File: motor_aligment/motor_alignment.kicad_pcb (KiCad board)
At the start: 2 copper layers, 110 x 80 mm, 25 parts, among them J1 PWR_24V_IN, J2 SENSOR_IN, J3 LCD_I2C, SW1 BTN, U1 LM2596S-5, U2 ADS1115, U3 ESP32-WROOM-32

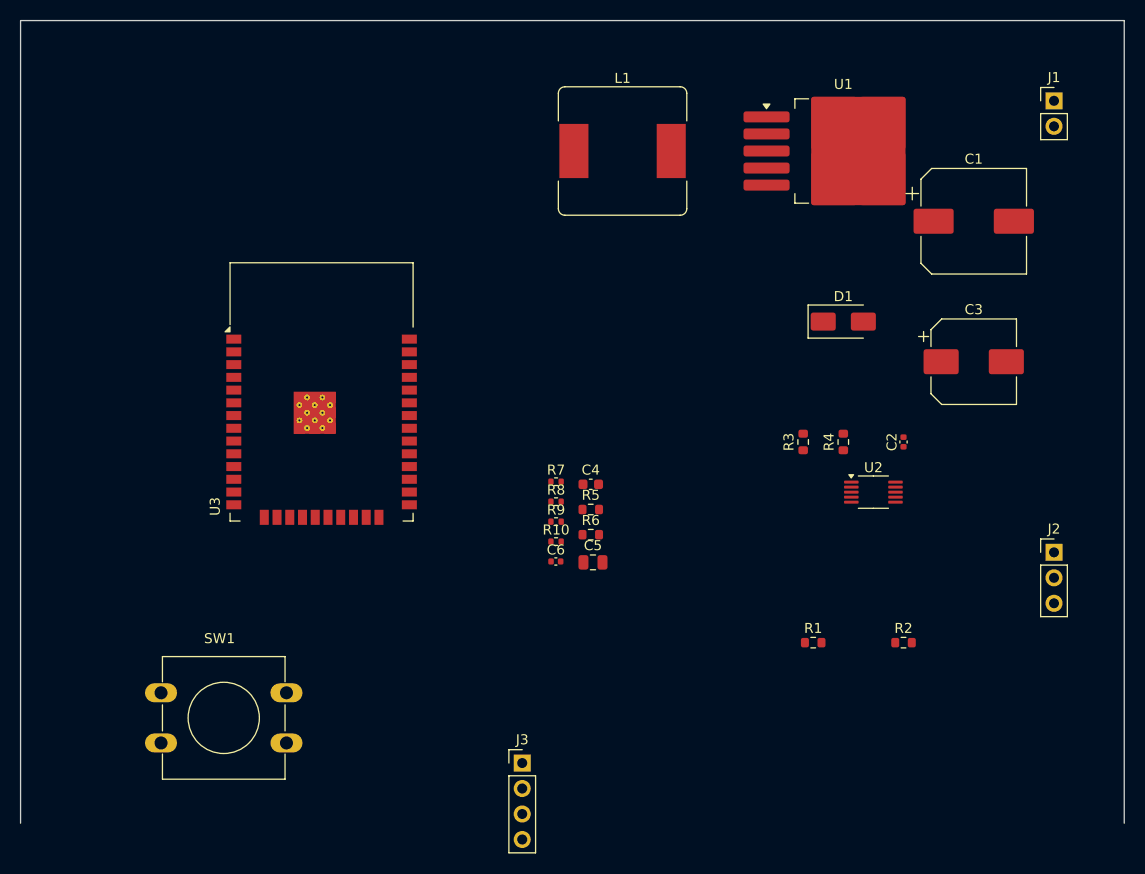
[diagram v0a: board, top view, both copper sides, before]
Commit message: Clean PCB layout: remove all traces/vias, fix component placement
- Remove all routing segments and vias (to be re-routed manually)
- Fix LCSC/MPN/Manufacturer/JLCPCB_Type properties on all 22 components
- Fix R7-R10 and C2/C6 footprints from 0402 to 0603
- Assign PinHeader_1x04 footprint to J4/J5
- Place components per LM2596 datasheet layout (pp. 31-32)
- Resolve courtyard overlaps and ESP32 antenna keepout violations
- DRC: 0 errors, 1 warning (lib_footprint_mismatch)

Co-Authored-By: Claude Sonnet 4.6 <noreply@anthropic.com>
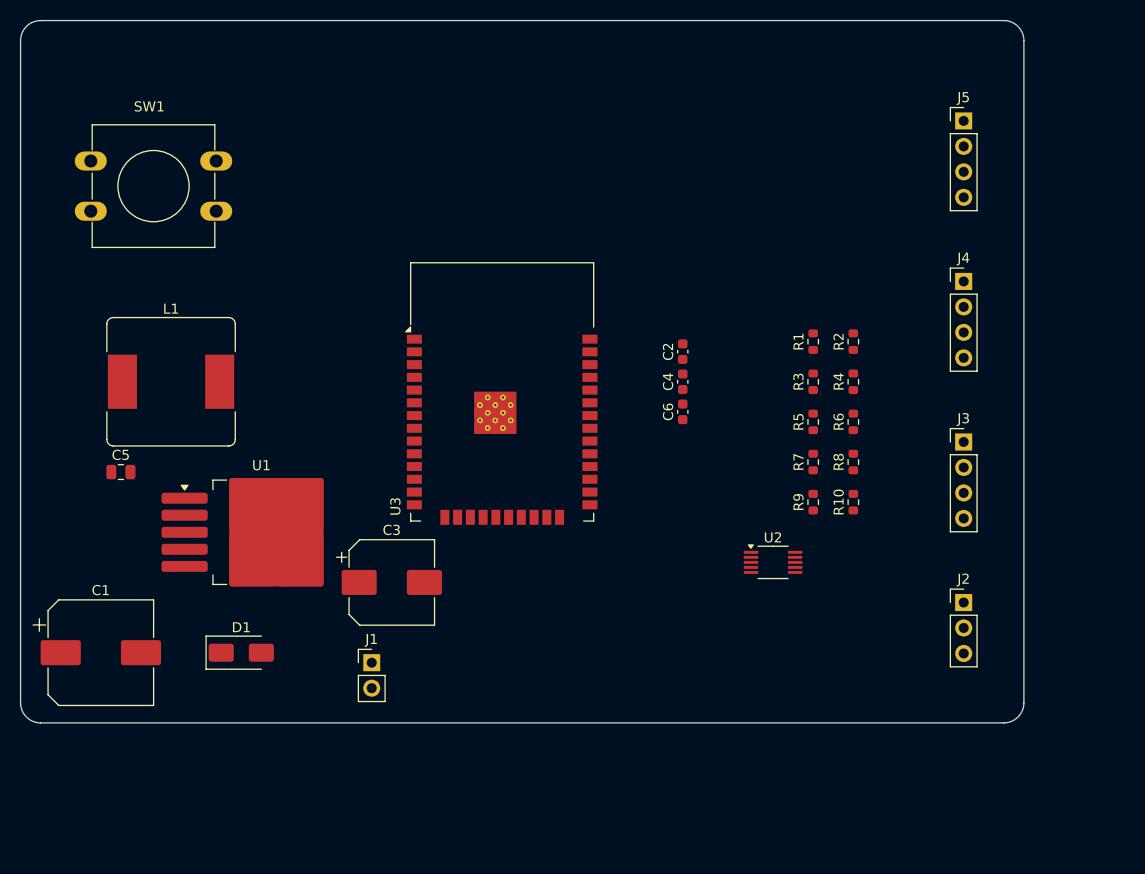
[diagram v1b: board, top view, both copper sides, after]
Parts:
- added J4: UART_DOWNLOAD, Connector_PinHeader_2.54mm:PinHeader_1x04_P2.54mm_Vertical, F.Cu at (94.0, 26.0)
- added J5: JTAG, Connector_PinHeader_2.54mm:PinHeader_1x04_P2.54mm_Vertical, F.Cu at (94.0, 10.0)
- C2, C6: footprint Capacitor_SMD:C_0402_1005Metric -> Capacitor_SMD:C_0603_1608Metric
- R10, R7, R8, R9: footprint Resistor_SMD:R_0402_1005Metric -> Resistor_SMD:R_0603_1608Metric
- moved C1 97.0 mm to (8.00, 63.0)
- moved J1 88.1 mm to (35.0, 64.0)
- moved U1 69.3 mm to (24.0, 51.0)
- moved D1 68.5 mm to (22.0, 63.0)
- moved C3 62.0 mm to (37.0, 56.0)
- moved J3 54.4 mm to (94.0, 42.0)
- moved SW1 53.5 mm to (7.00, 14.0)
- moved L1 50.5 mm to (15.0, 36.0)
- moved C5 47.9 mm to (10.0, 45.0)
- moved R2 30.4 mm to (83.0, 32.0), turned to 90 degrees
- moved R1 30.0 mm to (79.0, 32.0), turned to 90 degrees
- moved R8 29.9 mm to (83.0, 44.0), turned to 90 degrees
- moved R10 29.9 mm to (83.0, 48.0), turned to 90 degrees
- moved R6 28.5 mm to (83.0, 40.0), turned to 90 degrees
- moved R7 25.7 mm to (79.0, 44.0), turned to 90 degrees
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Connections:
- net /IO0_BOOT renamed Net-(U3-IO0)
- net /SCL renamed SCL
- net /SDA renamed SDA
- C1 pad 1: /+24V -> +24V
- C1 pad 2: /GND -> GND
- C2 pad 1: /+5V -> +5V
- C2 pad 2: /GND -> GND
- C3 pad 1: /+5V -> PWR_FLAG
- C3 pad 2: /GND -> GND
- C4 pad 2: /GND -> GND
- C5 pad 1: /+3.3V -> +3.3V
- C5 pad 2: /GND -> GND
- C6 pad 1: /+3.3V -> +3.3V
- C6 pad 2: /GND -> GND
- D1 pad 2: /GND -> GND
- J1 pad 1: /+24V -> PWR_FLAG
- J1 pad 2: /GND -> PWR_FLAG
- J2 pad 1: /+24V -> +24V
- J2 pad 3: /GND -> GND
- J3 pad 1: /+5V -> +5V
- J3 pad 2: /GND -> GND
- L1 pad 2: /+5V -> PWR_FLAG
- R10 pad 1: /JTAG_TDO -> Net-(U3-IO15)
- R10 pad 2: /IO15_JTAG -> /JTAG_TDO
- R2 pad 2: /GND -> GND
- R3 pad 1: /+3.3V -> +3.3V
- R4 pad 1: /+3.3V -> +3.3V
- R5 pad 1: /+3.3V -> PWR_FLAG
- R6 pad 1: /+3.3V -> +3.3V
- R7 pad 1: /JTAG_TDI -> Net-(U3-IO12)
- R7 pad 2: /IO12_JTAG -> /JTAG_TDI
- R8 pad 1: /JTAG_TMS -> Net-(U3-IO14)
- R8 pad 2: /IO14_JTAG -> /JTAG_TMS
- R9 pad 1: /JTAG_TCK -> Net-(U3-IO13)
- R9 pad 2: /IO13_JTAG -> /JTAG_TCK
- SW1 pad 2: /GND -> GND
- U1 pad 1: /+24V -> +24V
- U1 pad 3: /GND -> GND
- U1 pad 4: /+5V -> PWR_FLAG
- U1 pad 5: /GND -> GND
- U2 pad 1: /GND -> GND
- U2 pad 3: /GND -> GND
- U2 pad 8: /+5V -> +5V
- U3 pad 1: /GND -> GND
- U3 pad 13: /IO14_JTAG -> Net-(U3-IO14)
- U3 pad 14: /IO12_JTAG -> Net-(U3-IO12)
- U3 pad 15: /GND -> GND
- U3 pad 16: /IO13_JTAG -> Net-(U3-IO13)
- U3 pad 2: /+3.3V -> +3.3V
- U3 pad 23: /IO15_JTAG -> Net-(U3-IO15)
- U3 pad 37: unconnected-(U3-IO23-Pad37) -> /BTN
- U3 pad 38: /GND -> GND
- U3 pad 39: /GND -> GND
- U3 pad 8: /BTN -> unconnected-(U3-IO32-Pad8)
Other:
- board size 110 x 80 mm -> 100 x 70 mm

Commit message: Fix J4/J5 net assignments on PCB after schematic sync
J4 (UART_DOWNLOAD): pad1=+3.3V, pad2=UART_TX, pad3=UART_RX, pad4=GND
J5 (JTAG): pad1=JTAG_TDI, pad2=JTAG_TCK, pad3=JTAG_TMS, pad4=JTAG_TDO

Co-Authored-By: Claude Sonnet 4.6 <noreply@anthropic.com>
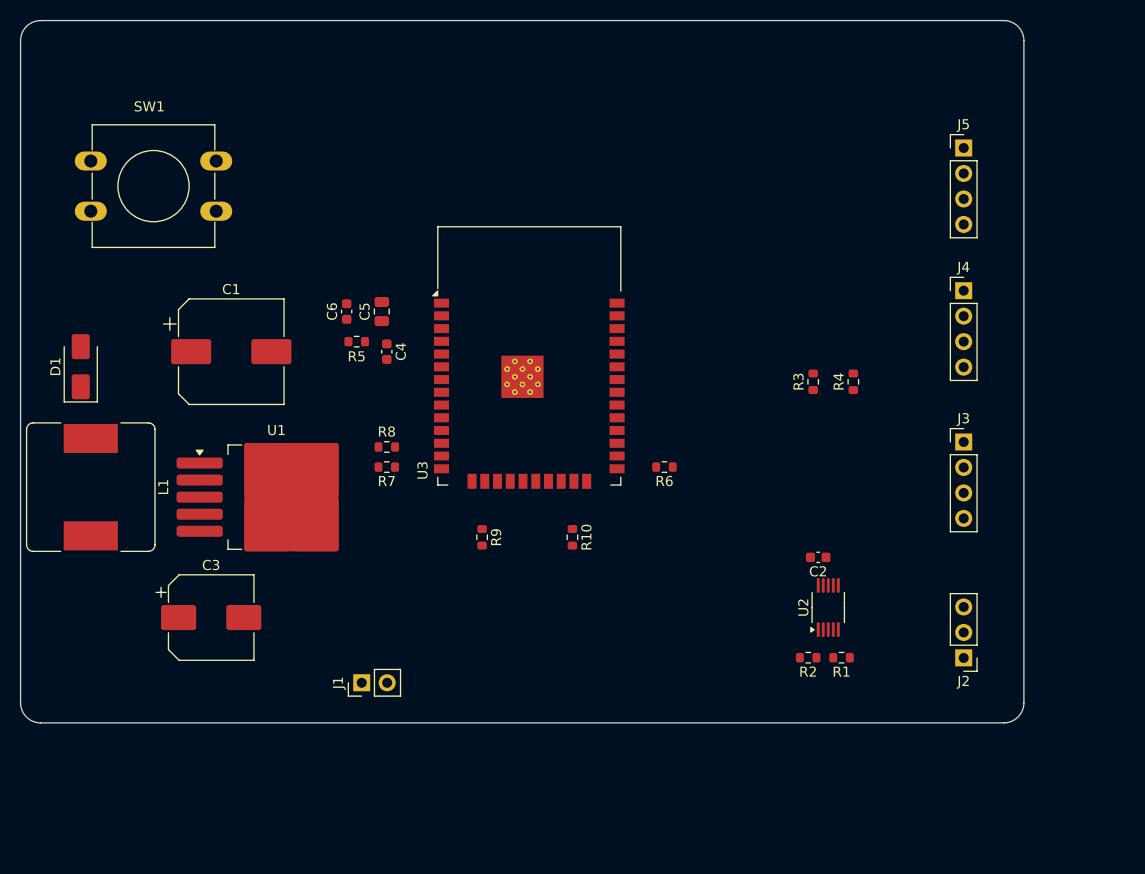
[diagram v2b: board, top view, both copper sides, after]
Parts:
- moved R8 46.5 mm to (36.5, 42.5), turned to 180 degrees
- moved R5 46.2 mm to (33.5, 32.0), turned to 0 degrees
- moved R7 42.5 mm to (36.5, 44.5), turned to 180 degrees
- moved C6 35.0 mm to (32.5, 29.0)
- moved R9 33.2 mm to (46.0, 51.5), turned to -90 degrees
- moved C1 32.7 mm to (21.0, 33.0)
- moved D1 32.7 mm to (6.00, 34.5), turned to 90 degrees
- moved R2 31.8 mm to (78.5, 63.5), turned to 180 degrees
- moved R1 31.6 mm to (81.8, 63.5), turned to 180 degrees
- moved C5 30.5 mm to (36.0, 29.0), turned to 90 degrees
- moved C4 29.7 mm to (36.5, 33.0), turned to -90 degrees
- moved R10 28.2 mm to (55.0, 51.5), turned to -90 degrees
- moved C2 24.5 mm to (79.5, 53.5), turned to 180 degrees
- moved R6 19.4 mm to (64.2, 44.5), turned to 180 degrees
- moved C3 18.3 mm to (19.0, 59.5)
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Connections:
- net SCL renamed /SCL
- net SDA renamed /SDA
- C1 pad 1: +24V -> /+24V
- C2 pad 1: +5V -> /+5V
- C3 pad 1: PWR_FLAG -> /+5V
- C5 pad 1: +3.3V -> /+3.3V
- C6 pad 1: +3.3V -> /+3.3V
- J1 pad 1: PWR_FLAG -> /+24V
- J1 pad 2: PWR_FLAG -> GND
- J2 pad 1: +24V -> /+24V
- J3 pad 1: +5V -> /+5V
- J4 pad 2: (no net) -> /UART_TX
- J4 pad 3: (no net) -> /UART_RX
- J5 pad 1: (no net) -> /JTAG_TDI
- J5 pad 2: (no net) -> /JTAG_TCK
- J5 pad 3: (no net) -> /JTAG_TMS
- J5 pad 4: (no net) -> /JTAG_TDO
- L1 pad 2: PWR_FLAG -> /+5V
- R3 pad 1: +3.3V -> /+3.3V
- R4 pad 1: +3.3V -> /+3.3V
- R5 pad 1: PWR_FLAG -> /+3.3V
- R6 pad 1: +3.3V -> /+3.3V
- U1 pad 1: +24V -> /+24V
- U1 pad 4: PWR_FLAG -> /+5V
- U2 pad 8: +5V -> /+5V
- U3 pad 2: +3.3V -> /+3.3V

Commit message: Update PCB, DSN/SES routing files and BOM export
Co-Authored-By: Claude Sonnet 4.6 <noreply@anthropic.com>
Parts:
- moved U3 11.1 mm to (61.8, 35.9)
- moved C4 11.0 mm to (47.5, 32.5)
- moved C5 11.0 mm to (47.0, 28.4)
- moved C6 11.0 mm to (43.5, 28.4)
- moved R10 11.0 mm to (66.0, 51.0)
- moved R5 11.0 mm to (44.5, 31.4)
- moved R6 11.0 mm to (75.2, 44.0)
- moved R7 11.0 mm to (47.5, 44.0)
- moved R8 11.0 mm to (47.5, 42.0)
- moved R9 11.0 mm to (57.0, 51.0)
- moved R4 9.64 mm to (75.5, 29.9), turned to 180 degrees
- moved R3 4.06 mm to (75.5, 34.0), turned to 180 degrees
- moved C1 3.54 mm to (24.5, 32.5)
- moved C3 3.54 mm to (22.5, 59.0)
- moved D1 3.54 mm to (9.50, 34.0)
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
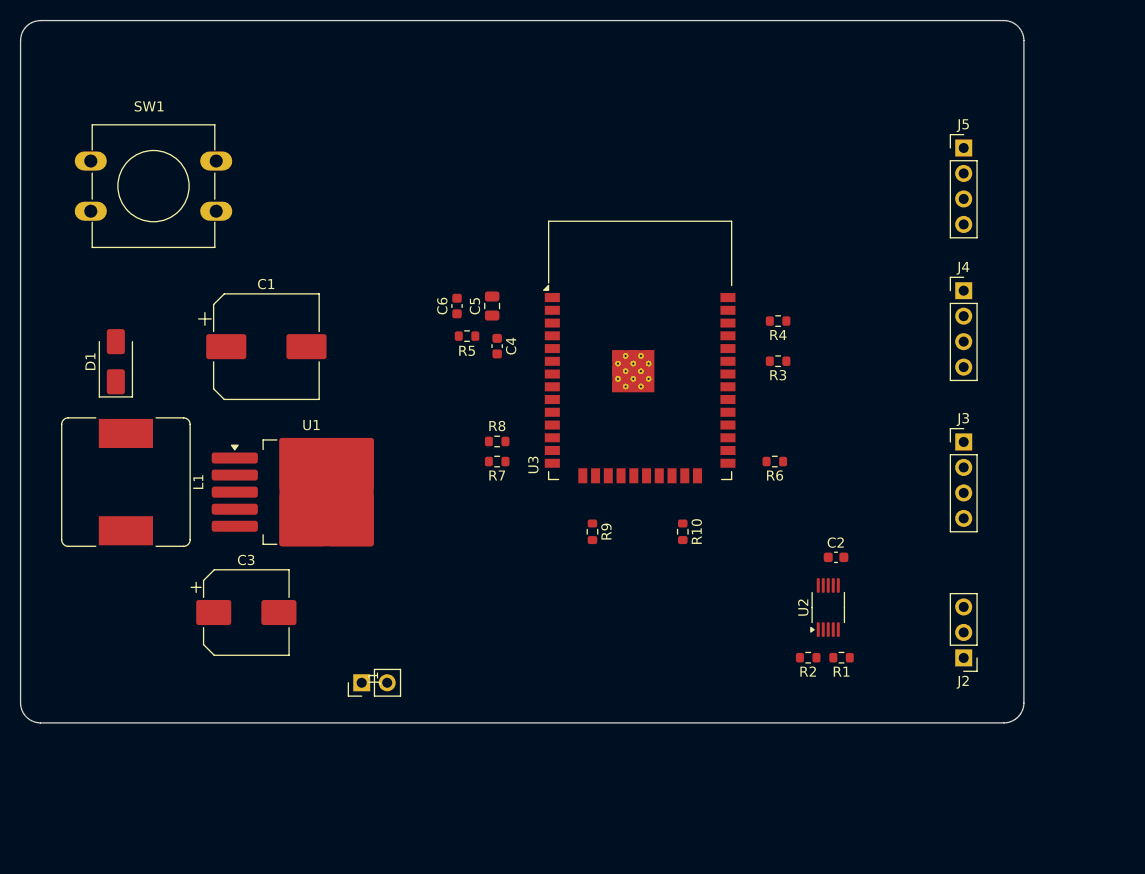
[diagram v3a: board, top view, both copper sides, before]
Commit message: Route all signal/power nets via Freerouting (GND excluded for copper pour)
- 160 tracks, 3 vias, 71 wire segments
- GND left unrouted (to be filled as copper pour)
- DRC: 0 errors, 3 warnings (silk cosmetic + lib_footprint_mismatch)

Co-Authored-By: Claude Sonnet 4.6 <noreply@anthropic.com>
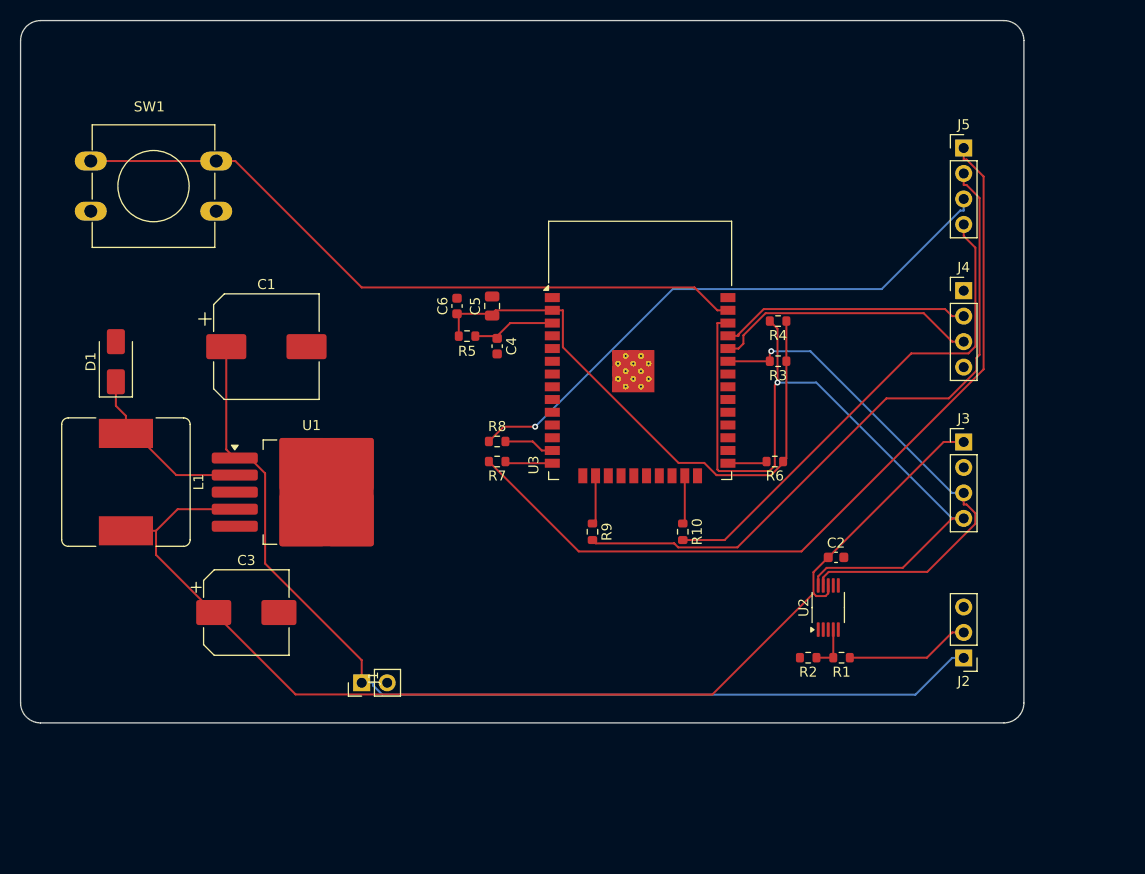
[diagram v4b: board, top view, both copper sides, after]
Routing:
- net /+5V: track 0.00 -> 114.6 mm
- net /+24V: track 0.00 -> 102.1 mm
- net /JTAG_TDI: track 0.00 -> 83.6 mm
- net /SCL: track 0.00 -> 78.5 mm, vias 0 -> 1
- net /BTN: track 0.00 -> 69.7 mm
- net /JTAG_TCK: track 0.00 -> 66.5 mm
- net /+3.3V: track 0.00 -> 58.8 mm
- net /JTAG_TMS: track 0.00 -> 58.0 mm, vias 0 -> 1
- net /SDA: track 0.00 -> 52.2 mm, vias 0 -> 1
- net /JTAG_TDO: track 0.00 -> 49.8 mm
- net /UART_RX: track 0.00 -> 26.6 mm
- net /UART_TX: track 0.00 -> 25.0 mm
- net Net-(D1-K): track 0.00 -> 18.5 mm
- net /SENSOR_OUT: track 0.00 -> 12.4 mm
- net /ESP32_EN: track 0.00 -> 8.44 mm
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
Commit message: Add GND copper pour on F.Cu and B.Cu
- Solid fill on SMD pads (thru_hole_only thermal relief)
- Thermal gap 0.1mm, bridge width 0.15mm
- DRC: 0 errors, 3 warnings (silk cosmetic + lib_footprint_mismatch)

Co-Authored-By: Claude Sonnet 4.6 <noreply@anthropic.com>
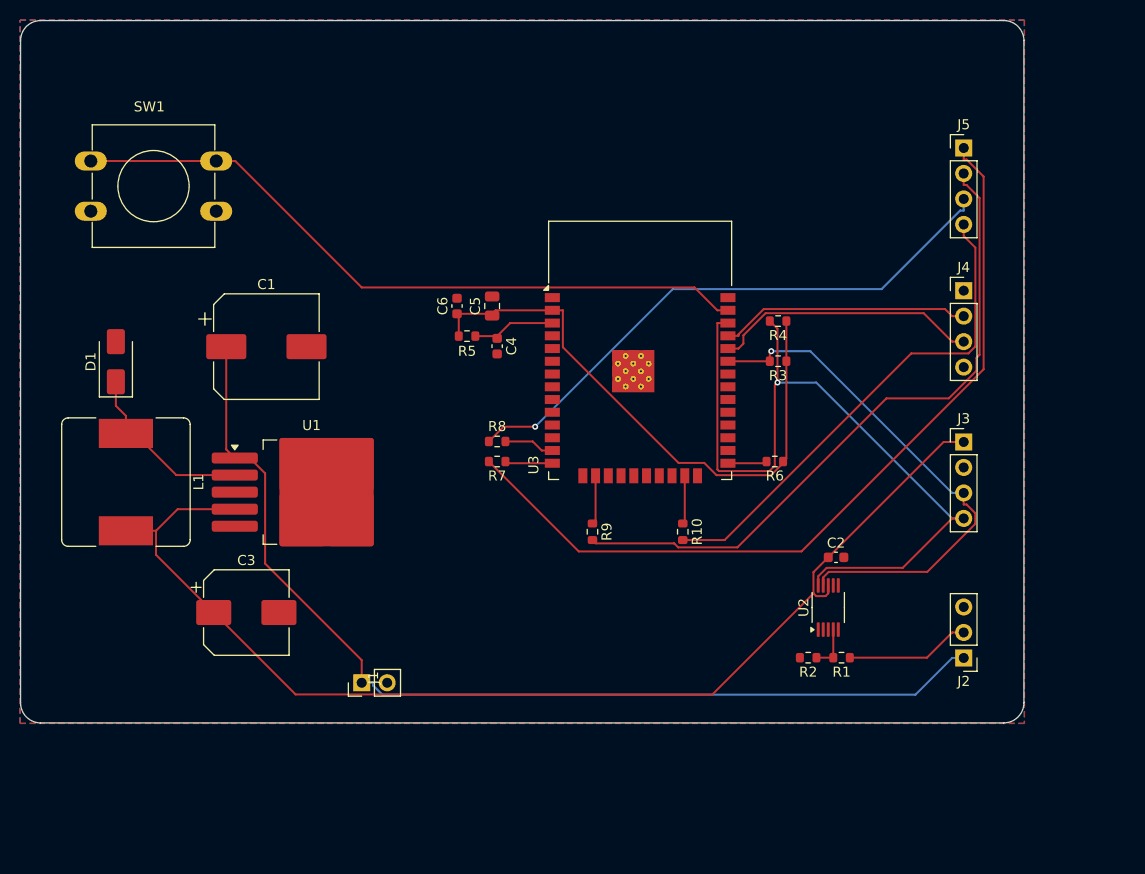
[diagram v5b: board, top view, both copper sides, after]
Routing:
- added copper zone on B.Cu, net GND
- added copper zone on F.Cu, net GND
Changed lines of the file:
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@@
 		(net 50)
 	)
+	(zone
+		(net 10)
+		(net_name "GND")
+		(layer "F.Cu")
+		(hatch edge 0.5)
+		(connect_pads thru_hole_only
+			(clearance 0.3)
+		)
+		(min_thickness 0.2)
+		(filled_areas_thickness no)
+		(fill yes
+			(thermal_gap 0.1)
+			(thermal_bridge_width 0.15)
+		)
+		(polygon
+			(pts
+				(xy -0.05 -0.05) (xy 100.05 -0.05) (xy 100.05 70.05) (xy -0.05 70.05)
+			)
+		)
+	)
+	(zone
+		(net 10)
+		(net_name "GND")
+		(layer "B.Cu")
+		(hatch edge 0.5)
+		(connect_pads thru_hole_only
+			(clearance 0.3)
+		)
+		(min_thickness 0.2)
+		(filled_areas_thickness no)
+		(fill yes
+			(thermal_gap 0.1)
+			(thermal_bridge_width 0.15)
+		)
+		(polygon
+			(pts
+				(xy -0.05 -0.05) (xy 100.05 -0.05) (xy 100.05 70.05) (xy -0.05 70.05)
+			)
+		)
+	)
 )
